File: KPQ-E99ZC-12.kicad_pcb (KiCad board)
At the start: 2 copper layers, 79.2 x 53 mm, 25 parts, among them J1 USB Cable, J2 Chassis, J3 SWD, J4 Edge Connector, J5 Alternate Connector 1, J6 Alternate Connector 2, SW1 BOOT, U1 USBLC6-2SC6, U2 XC6206P332MR-G, U3 STM32C071KBT6

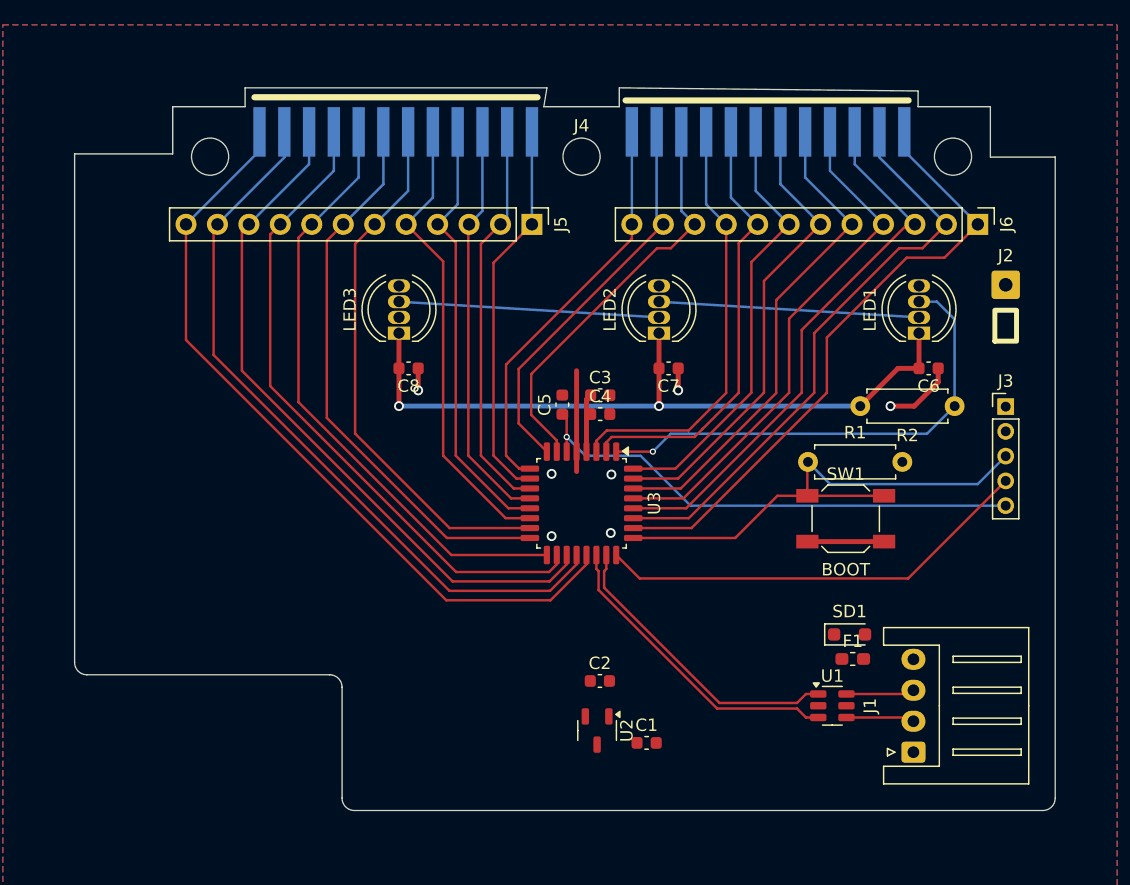
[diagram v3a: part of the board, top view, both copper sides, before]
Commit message: Refine edges and positioning, especially around edge connectors
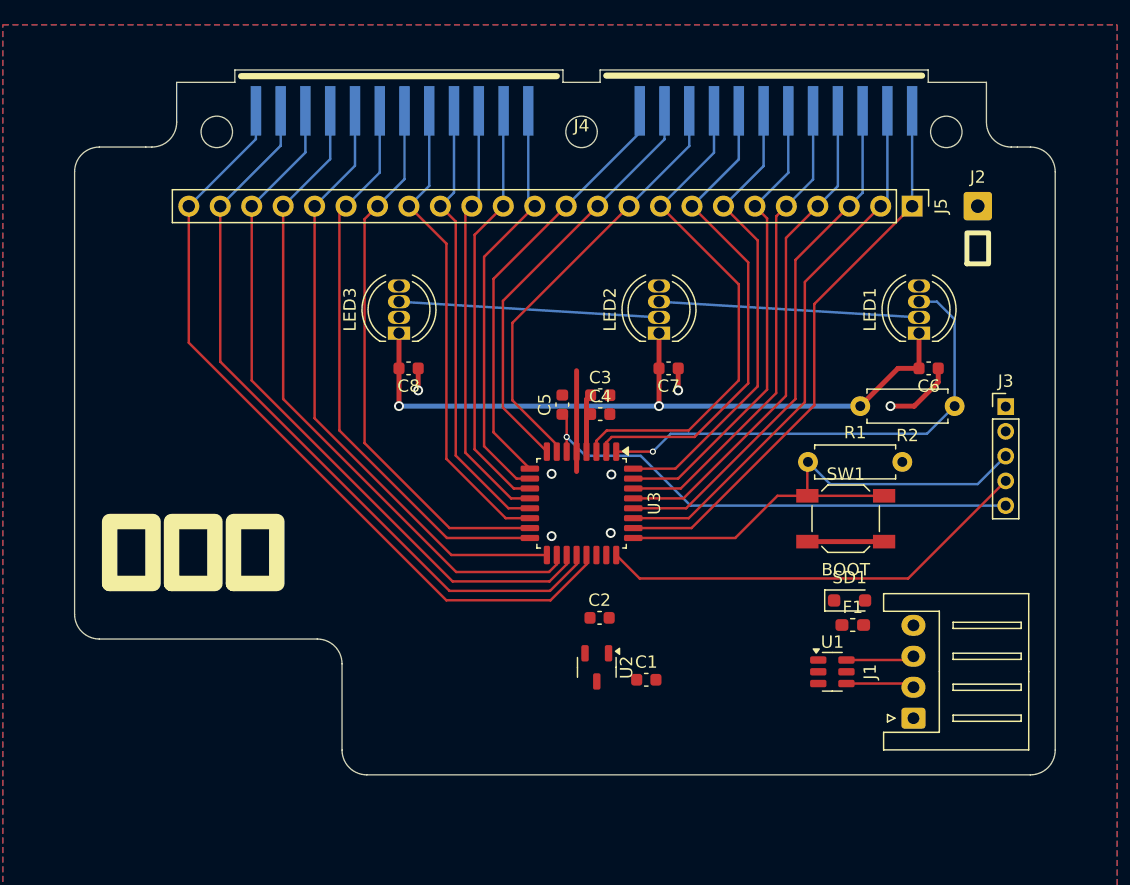
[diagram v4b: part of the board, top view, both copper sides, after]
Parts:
- removed J6: Alternate Connector 2, Connector_PinHeader_2.54mm:PinHeader_1x12_P2.54mm_Vertical
- J5: value Alternate Connector 1 -> Alternate Connector; footprint Connector_PinHeader_2.54mm:PinHeader_1x12_P2.54mm_Vertical -> Connector_PinHeader_2.54mm:PinHeader_1x24_P2.54mm_Vertical
- moved J5 30.7 mm to (126.7, 106.0)
- moved J2 6.74 mm to (132.0, 106.0)
- moved C1 5.10 mm to (105.2, 144.3)
- moved C2 5.10 mm to (101.5, 139.3)
- moved U2 5.10 mm to (101.2, 143.3)
- moved F1 2.74 mm to (121.9, 139.8)
- moved J1 2.74 mm to (126.8, 147.4)
- moved SD1 2.74 mm to (121.6, 137.8)
- moved U1 2.74 mm to (120.3, 143.6)
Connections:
- J5 pad 1: Col5 -> Row1
- J5 pad 10: Col14 -> Col2
- J5 pad 11: Col15 -> Col3
- J5 pad 12: Col16 -> Col4
- J5 pad 2: Col6 -> Row2
- J5 pad 3: Col7 -> Row3
- J5 pad 4: Col8 -> Row4
- J5 pad 5: Col9 -> Row5
- J5 pad 6: Col10 -> Row6
- J5 pad 7: Col11 -> Row7
- J5 pad 8: Col12 -> Row8
- J5 pad 9: Col13 -> Col1
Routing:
- net USB_D-: track 24.9 -> 0.00 mm
- net USB_D+: track 24.2 -> 0.00 mm
- net Col1: track 34.7 -> 40.9 mm
- net Row8: track 35.7 -> 39.9 mm
- net Row2: track 47.6 -> 44.3 mm
- net Col5: track 31.1 -> 34.1 mm
- net Col16: track 60.7 -> 63.7 mm
- net Row1: track 49.0 -> 46.1 mm
- net Col3: track 31.8 -> 34.7 mm
- net Row7: track 35.5 -> 37.8 mm
- net Col6: track 32.1 -> 34.4 mm
- net Col4: track 32.7 -> 35.0 mm
- net Col7: track 32.9 -> 35.1 mm
- net Row3: track 44.7 -> 42.6 mm
- net Col2: track 33.3 -> 35.2 mm
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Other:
- board size 79.2 x 53 mm -> 79.2 x 50.7 mm
- board text added: "ミツミ"

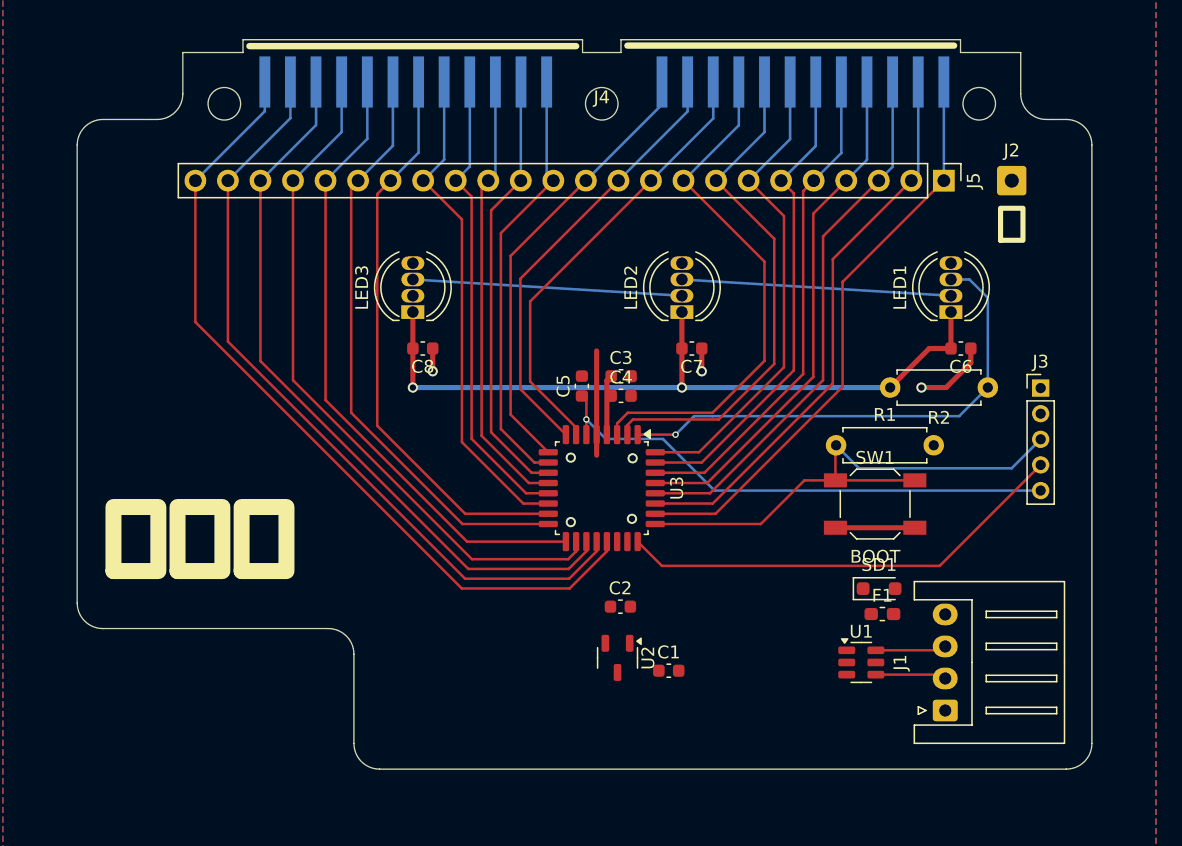
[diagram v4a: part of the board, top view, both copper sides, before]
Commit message: Add +5V to SWD port, label SWD port, adjust PCB outline
PCB outline and LED placement adjusted after comparing printout with actual PCB.
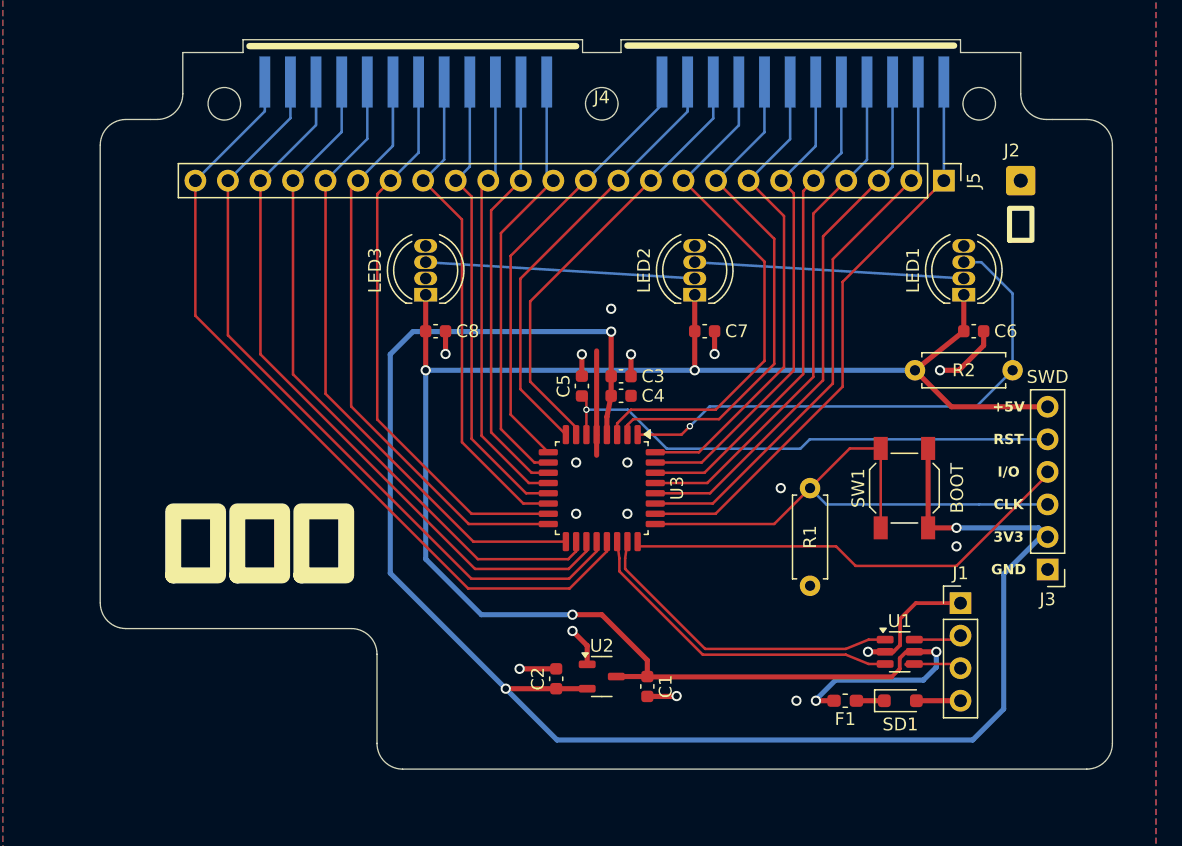
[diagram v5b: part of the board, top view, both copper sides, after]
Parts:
- J1: footprint Connector_JST:JST_XH_S4B-XH-A_1x04_P2.50mm_Horizontal -> Connector_PinHeader_2.54mm:PinHeader_1x04_P2.54mm_Vertical
- J3: footprint Connector_PinHeader_2.00mm:PinHeader_1x05_P2.00mm_Vertical -> Project_Library:PinHeader_1x06_P2.54mm_Vertical
- moved J3 14.2 mm to (134.8, 136.3), turned to 180 degrees
- moved SD1 8.90 mm to (123.3, 146.6)
- moved J1 8.47 mm to (128.0, 139.0), turned to 0 degrees
- moved C2 7.54 mm to (96.4, 144.9), turned to 90 degrees
- moved F1 7.36 mm to (119.0, 146.6), turned to 180 degrees
- moved R1 3.91 mm to (116.3, 130.0), turned to -90 degrees
- moved U1 3.11 mm to (123.3, 142.8)
- moved SW1 2.60 mm to (123.6, 130.0), turned to 90 degrees
- moved R2 2.36 mm to (132.1, 120.8)
- moved C1 2.08 mm to (103.6, 145.5), turned to -90 degrees
- moved U2 1.90 mm to (100.0, 144.7), turned to 0 degrees
- moved C6 1.68 mm to (129.0, 117.8)
- moved C7 1.68 mm to (108.0, 117.8)
- moved C8 1.68 mm to (87.0, 117.8)
- moved LED1 1.68 mm to (128.3, 114.9)
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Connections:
- J1 pad 2: USBP_D- -> USBP_D+
- J1 pad 3: USBP_D+ -> USBP_D-
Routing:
- net +3V3: track 10.9 -> 134.8 mm, vias 0 -> 3
- net +5V: track 57.9 -> 144.5 mm, vias 2 -> 5
- net USB_D-: track 0.00 -> 25.9 mm
- net USB_D+: track 0.00 -> 25.2 mm
- net GND: track 17.5 -> 38.7 mm, vias 7 -> 17
- net VBUS: track 0.00 -> 3.44 mm
- net BOOT0/SWCLK: track 42.1 -> 45.3 mm
- net LED: track 39.3 -> 42.2 mm
- net Net-(SD1-K): track 0.00 -> 2.18 mm
- net USBP_D+: track 5.11 -> 3.30 mm
- net Col4: track 35.0 -> 33.2 mm
- net USBP_D-: track 5.11 -> 3.91 mm
- net Col7: track 35.1 -> 34.4 mm
- net Col5: track 34.1 -> 33.3 mm
- net Col2: track 35.2 -> 34.7 mm
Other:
- board size 79.2 x 50.7 mm -> 79 x 50.7 mm

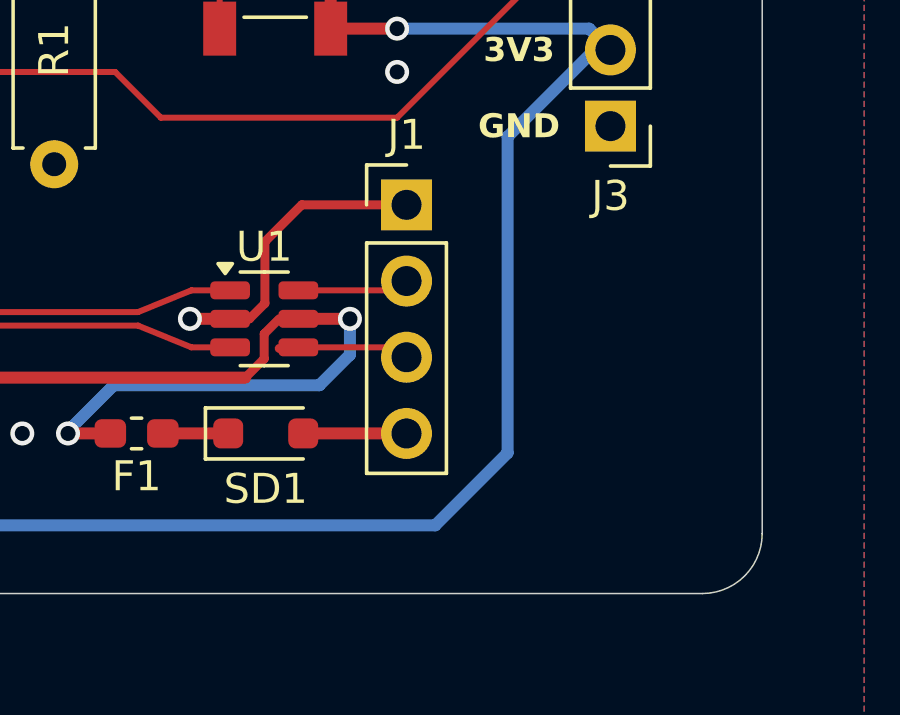
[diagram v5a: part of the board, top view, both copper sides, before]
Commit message: Label USB post pins
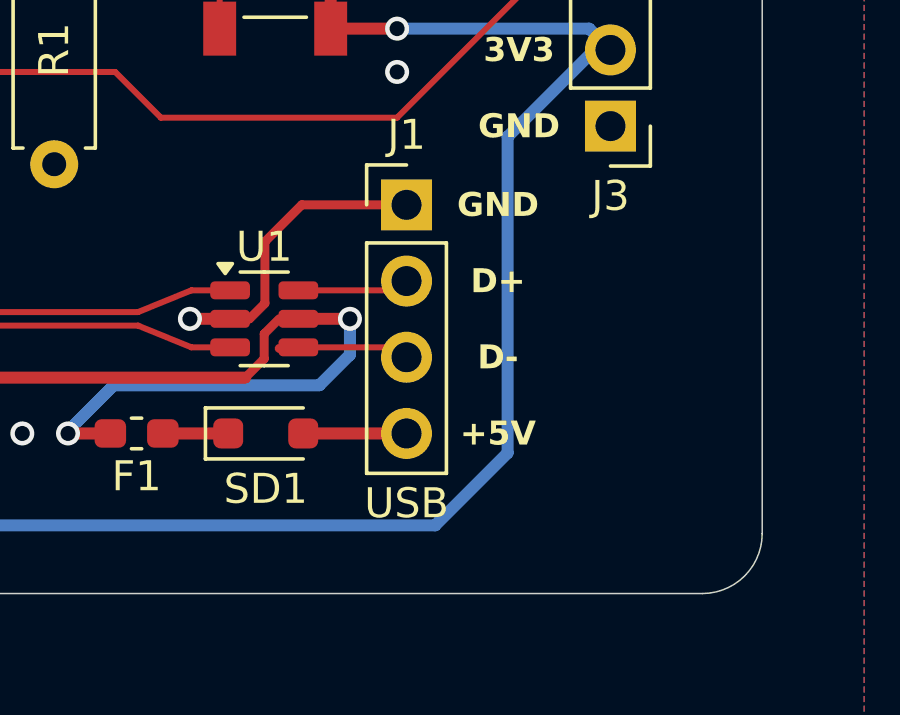
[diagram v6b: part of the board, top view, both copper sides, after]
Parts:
- J1: value USB Cable -> USB; footprint Connector_PinHeader_2.54mm:PinHeader_1x04_P2.54mm_Vertical -> Project_Library:PinHeader_1x04_P2.54mm_Vertical
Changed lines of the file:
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@@
 	(net 39 "USB_D+")
 	(net 40 "Net-(SD1-K)")
-	(footprint "Connector_PinHeader_2.54mm:PinHeader_1x04_P2.54mm_Vertical"
+	(footprint "Project_Library:PinHeader_1x04_P2.54mm_Vertical"
 		(layer "F.Cu")
 		(at 128 138.973355)
@@
 			)
 		)
-		(property "Value" "USB Cable"
+		(property "Value" "USB"
 			(at 0 9.95 0)
-			(layer "F.Fab")
+			(layer "F.SilkS")
 			(effects
 				(font
@@
 				(font
 					(size 1.27 1.27)
+					(thickness 0.15)
+				)
+			)
+		)
+		(property "P1" "GND"
+			(at 0 0 0)
+			(unlocked yes)
+			(layer "F.Fab")
+			(hide yes)
+			(effects
+				(font
+					(size 1 1)
+					(thickness 0.15)
+				)
+			)
+		)
+		(property "P2" "D+"
+			(at 0 0 0)
+			(unlocked yes)
+			(layer "F.Fab")
+			(hide yes)
+			(effects
+				(font
+					(size 1 1)
+					(thickness 0.15)
+				)
+			)
+		)
+		(property "P3" "D-"
+			(at 0 0 0)
+			(unlocked yes)
+			(layer "F.Fab")
+			(hide yes)
+			(effects
+				(font
+					(size 1 1)
+					(thickness 0.15)
+				)
+			)
+		)
+		(property "P4" "+5V"
+			(at 0 0 0)
+			(unlocked yes)
+			(layer "F.Fab")
+			(hide yes)
+			(effects
+				(font
+					(size 1 1)
 					(thickness 0.15)
 				)
@@
 			(layer "F.Fab")
 		)
+		(fp_text user "${P1}"
+			(at 3.048 0 0)
+			(layer "F.SilkS")
+			(effects
+				(font
+					(size 0.8 0.8)
+					(thickness 0.16)
+					(bold yes)
+				)
+			)
+		)
+		(fp_text user "${P2}"
+			(at 3.048 2.54 0)
+			(layer "F.SilkS")
+			(effects
+				(font
+					(size 0.8 0.8)
+					(thickness 0.16)
+					(bold yes)
+				)
+			)
+		)
+		(fp_text user "${P4}"
+			(at 3.048 7.62 0)
+			(layer "F.SilkS")
+			(effects
+				(font
+					(size 0.8 0.8)
+					(thickness 0.16)
+					(bold yes)
+				)
+			)
+		)
+		(fp_text user "${P3}"
+			(at 3.048 5.08 0)
+			(layer "F.SilkS")
+			(effects
+				(font
+					(size 0.8 0.8)
+					(thickness 0.16)
+					(bold yes)
+				)
+			)
+		)
 		(fp_text user "${REFERENCE}"

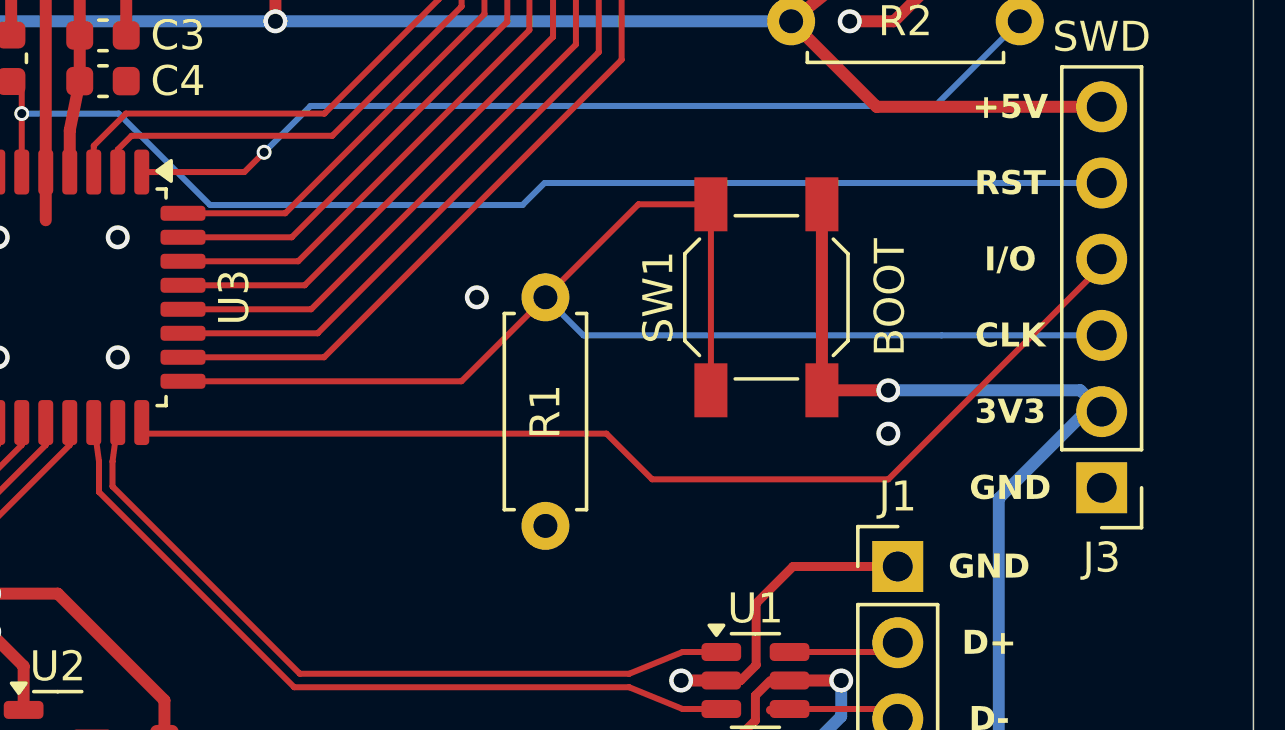
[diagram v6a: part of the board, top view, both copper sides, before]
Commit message: Remove pull-down resistor on BOOT0
Since pin 25 is also a GPIO pin it has an internal pull-down resistor. The resistor is engaged on reset to allow for SWCLK functionality.
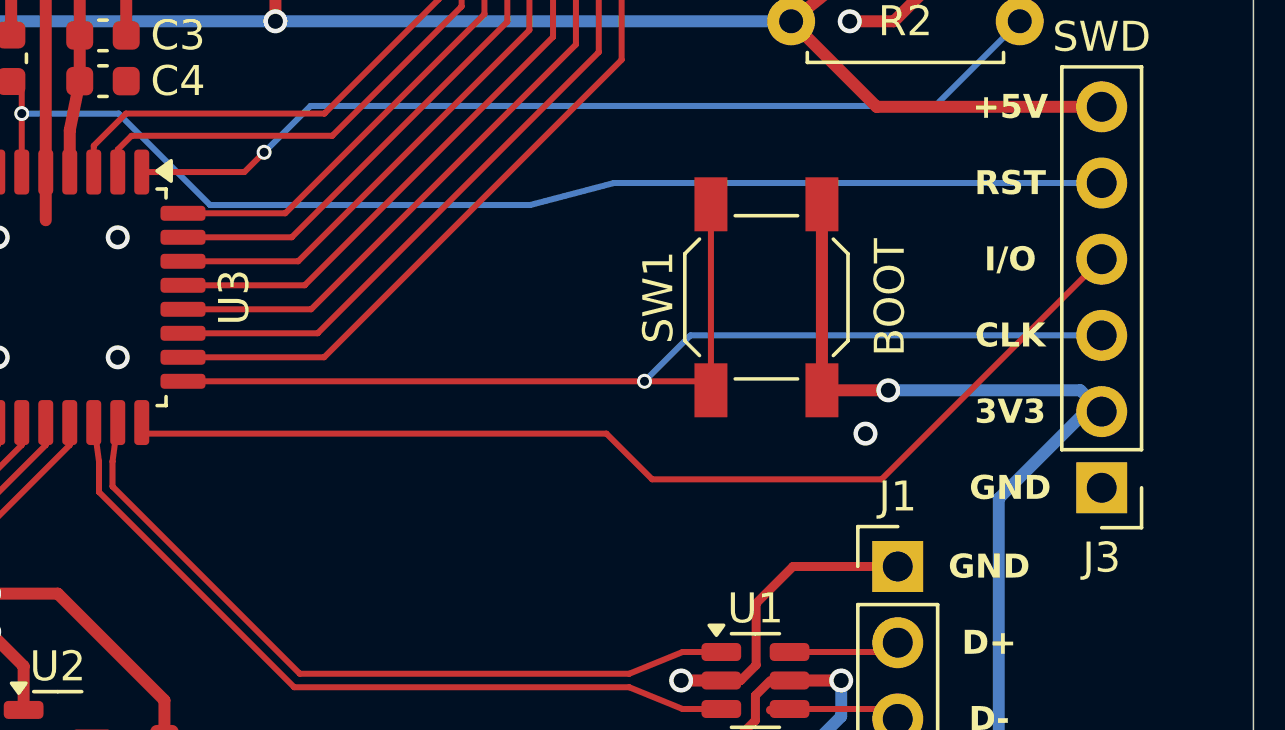
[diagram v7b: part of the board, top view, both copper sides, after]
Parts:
- removed R1: 10kΩ, Resistor_THT:R_Axial_DIN0207_L6.3mm_D2.5mm_P7.62mm_Horizontal
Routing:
- net BOOT0/SWCLK: track 45.3 -> 39.8 mm, vias 0 -> 1
- net GND: vias 17 -> 16
